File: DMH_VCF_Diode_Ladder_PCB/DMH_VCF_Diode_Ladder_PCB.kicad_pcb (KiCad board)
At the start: 2 copper layers, 96 x 157.5 mm, 68 parts, among them J0 Conn_01x01, J100 IDC_02x08, J200 IDC_02x05, J50 Conn_01x06, J60 Conn_01x06, SW1 SW_SPDT, SW2 SW_SPDT, SW3 SW_SPDT, SW4 SW_SPDT_321_OnOff, U1 TL074, U2 TL074

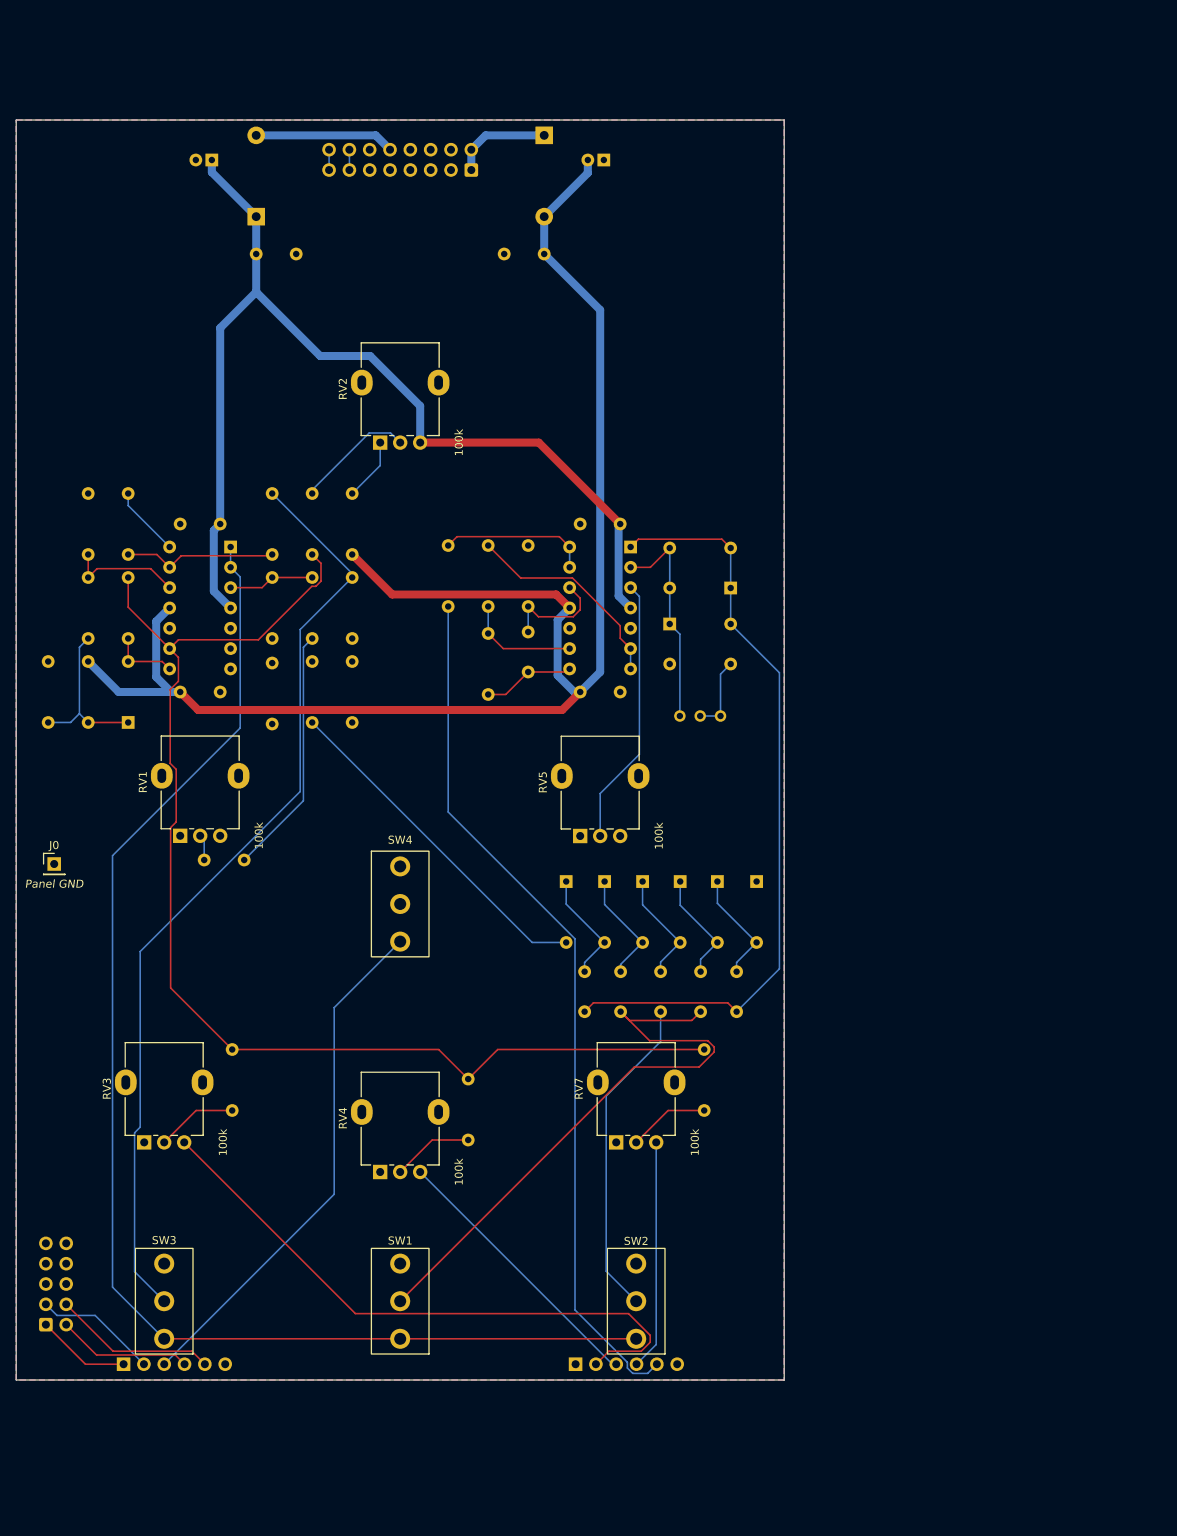
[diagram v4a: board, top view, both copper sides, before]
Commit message: Main PCB routing done
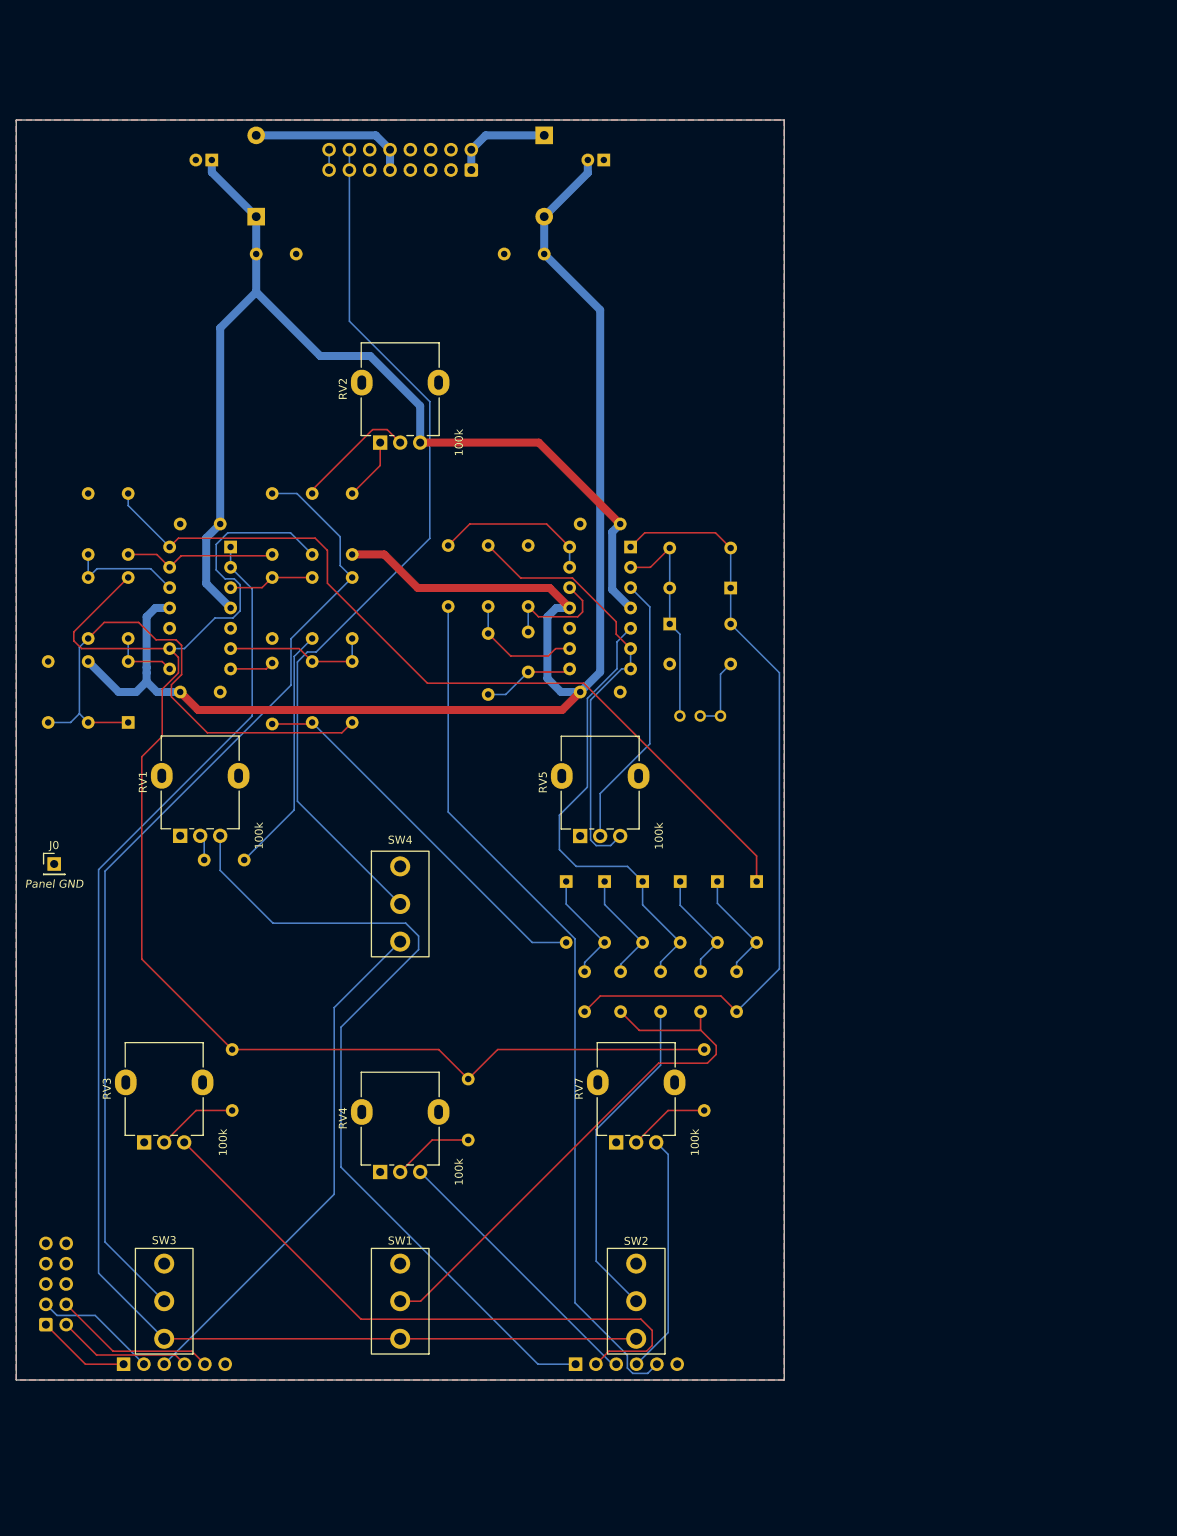
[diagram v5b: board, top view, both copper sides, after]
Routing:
- net /Inputs and Outputs/Bus CV In: track 2.54 -> 111.3 mm
- net /Core Circuit/Input: track 0.00 -> 105.0 mm
- net Net-(D12-K): track 8.83 -> 104.7 mm
- net Net-(D6-K): track 20.8 -> 66.4 mm
- net Net-(D10-A): track 14.2 -> 57.6 mm
- net Net-(U2B--): track 26.6 -> 55.2 mm
- net Net-(U1C--): track 154.1 -> 177.0 mm
- net Net-(U1B--): track 0.00 -> 18.7 mm
- net Net-(SW1-B): track 77.2 -> 69.4 mm
- net Net-(R17-Pad1): track 0.00 -> 5.50 mm
- net Net-(D7-A): track 43.1 -> 48.2 mm
- net Net-(SW3-B): track 117.9 -> 122.8 mm
- net Net-(SW1-C): track 167.8 -> 170.4 mm
- net Net-(D1-A): track 17.5 -> 20.0 mm
- net -12V: track 193.4 -> 195.8 mm
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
